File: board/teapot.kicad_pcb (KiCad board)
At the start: 2 copper layers, 49.9 x 50 mm, 41 parts, among them J1 MICROUSB, P1 BATT, P2 SMA, Q1 TEPT4400, U1 TPS79333DBVR, U2 TLV61225, U4 RFM69W, U5 STM32L052K8, U6 HTU21D, U7 MS5637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

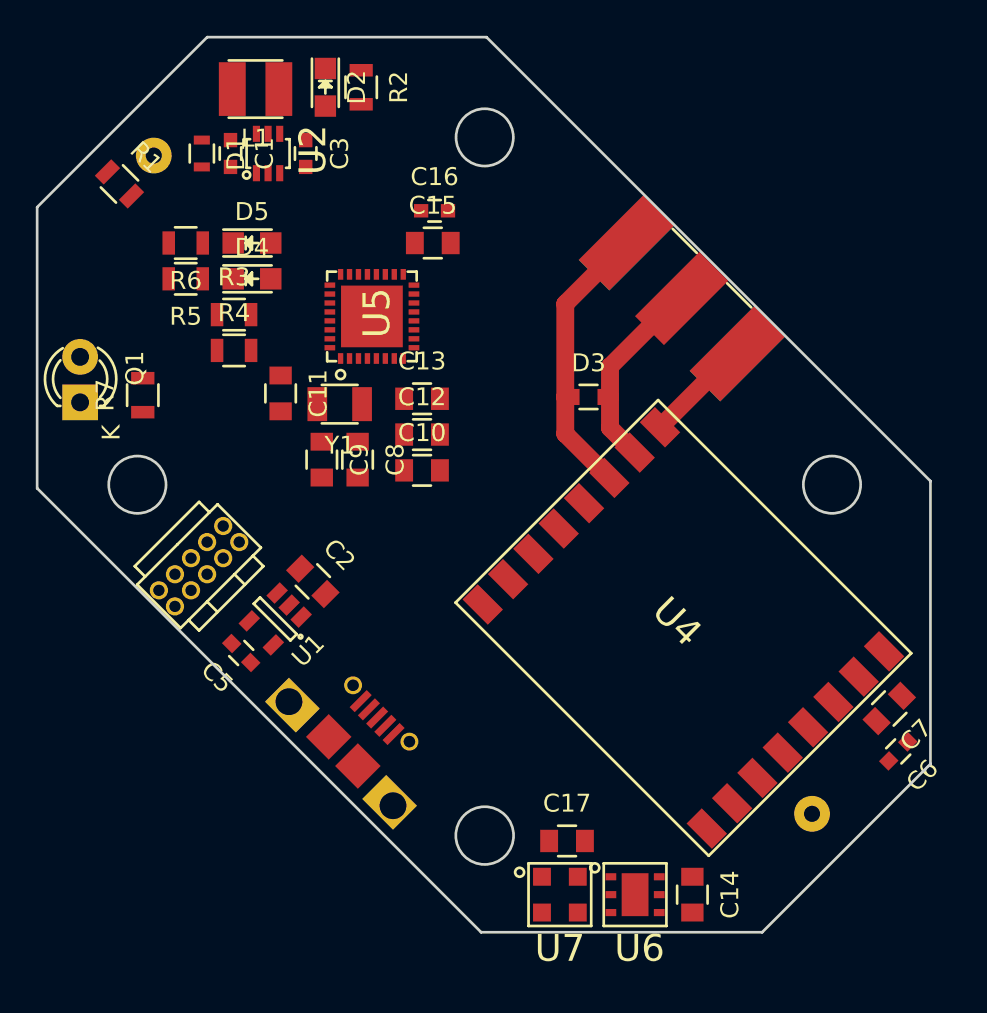
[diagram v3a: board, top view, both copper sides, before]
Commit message: Added test points and ANT PTH footprint
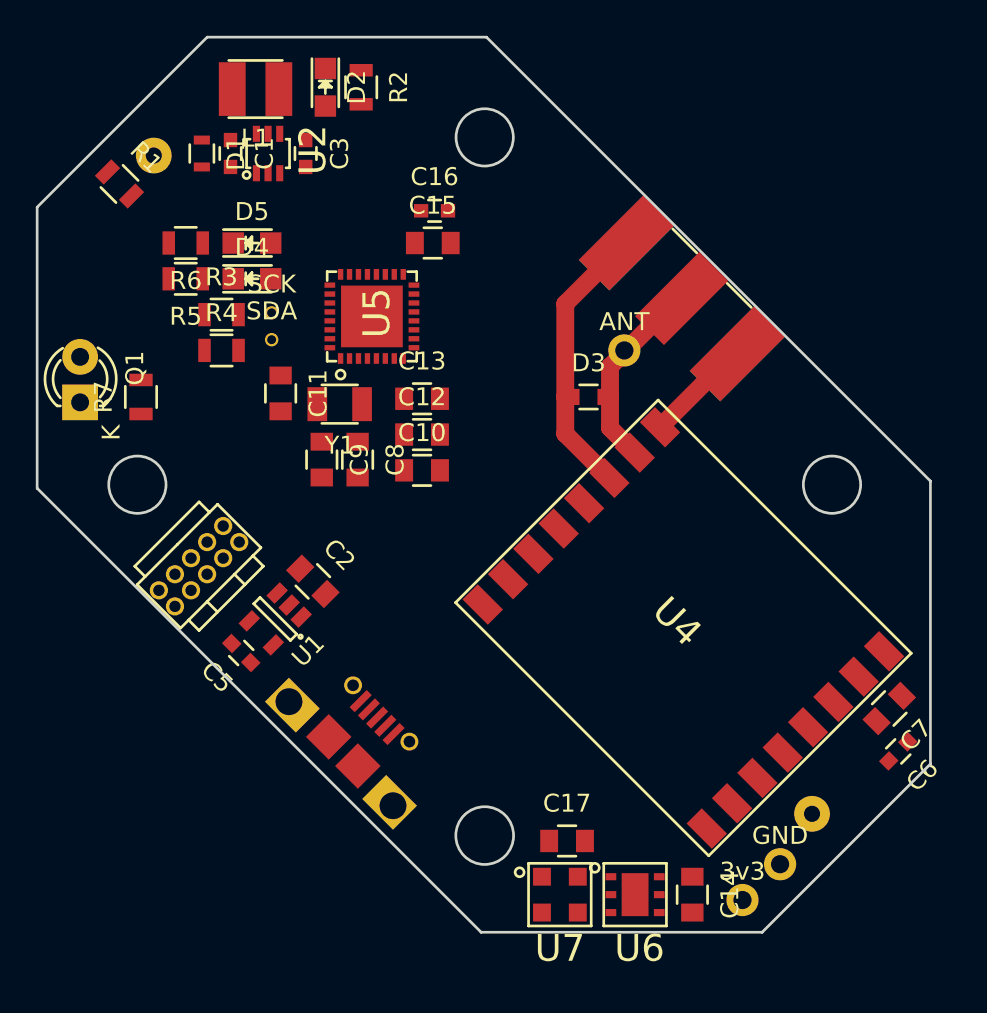
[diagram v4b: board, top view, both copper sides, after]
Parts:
- added TP1: ANT, footprints:Test_point, F.Cu at (134.8, 105.5)
- added TP2: 3v3, footprints:Test_point, F.Cu at (141.4, 136.2)
- added TP3: GND, footprints:Test_point, F.Cu at (143.5, 134.2)
- added TP4: SCK, footprints:Test_point_mini, F.Cu at (115.1, 103.4)
- added TP5: SDA, footprints:Test_point_mini, F.Cu at (115.1, 104.9)
- moved R3 0.70 mm to (112.3, 103.5)
- moved R4 0.70 mm to (112.3, 105.5)
- moved R7 0.14 mm to (107.8, 108.1)
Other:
- net class Default: clearance 0.2 -> 0.15
- rule trace_clearance: 0.2 -> 0.15
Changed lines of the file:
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@@
 (kicad_pcb (version 4) (host pcbnew 4.0.1-3.201512150931+6195~38~ubuntu14.04.1-stable)
   (general
-    (links 109)
-    (no_connects 104)
+    (links 114)
+    (no_connects 109)
     (area 101.924999 87.924999 151.975001 138.075001)
     (thickness 1.6)
@@
     (tracks 17)
     (zones 0)
-    (modules 41)
+    (modules 46)
     (nets 30)
   )
@@
     (user_trace_width 0.75)
     (user_trace_width 1)
-    (trace_clearance 0.2)
+    (trace_clearance 0.15)
     (zone_clearance 0.5)
     (zone_45_only no)
@@
   (net 29 "Net-(J1-PadS)")
   (net_class Default "This is the default net class."
-    (clearance 0.2)
+    (clearance 0.15)
     (trace_width 0.25)
     (via_dia 0.7)
@@
   )
   (module Resistors_SMD:R_0805 (layer F.Cu)
-    (at 113 103.5)
+    (at 112.3 103.5)
     (descr "Resistor SMD 0805, reflow soldering, Vishay (see dcrcw.pdf)")
     (tags "resistor 0805")
@@
   )
   (module Resistors_SMD:R_0805 (layer F.Cu)
-    (at 113 105.5)
+    (at 112.3 105.5)
     (descr "Resistor SMD 0805, reflow soldering, Vishay (see dcrcw.pdf)")
     (tags "resistor 0805")
@@
   )
   (module Resistors_SMD:R_0805 (layer F.Cu)
-    (at 107.9 108 90)
+    (at 107.8 108.1 90)
     (descr "Resistor SMD 0805, reflow soldering, Vishay (see dcrcw.pdf)")
     (tags "resistor 0805")
@@
       (net 29 "Net-(J1-PadS)"))
   )
+  (module footprints:Test_point (layer F.Cu)
+    (at 134.8 105.5)
+    (descr "Test Point")
+    (tags "test point")
+    (fp_text reference TP1 (at 0 2) (layer F.SilkS) hide
+      (effects (font (size 1 1) (thickness 0.15)))
+    )
+    (fp_text value ANT (at 0 -1.6) (layer F.SilkS)
+      (effects (font (size 1 1) (thickness 0.15)))
+    )
+    (pad 1 thru_hole circle (at 0 0) (size 1.8 1.8) (drill 1.016) (layers *.Cu *.Mask F.SilkS)
+      (net 16 "Net-(D3-Pad2)"))
+    (model Pin_Headers.3dshapes/Pin_Header_Straight_1x01.wrl
+      (at (xyz 0 0 0))
+      (scale (xyz 1 1 1))
+      (rotate (xyz 0 0 90))
+    )
+  )
+  (module footprints:Test_point (layer F.Cu)
+    (at 141.4 136.2)
+    (descr "Test Point")
+    (tags "test point")
+    (fp_text reference TP2 (at 0 2) (layer F.SilkS) hide
+      (effects (font (size 1 1) (thickness 0.15)))
+    )
+    (fp_text value 3v3 (at 0 -1.6) (layer F.SilkS)
+      (effects (font (size 1 1) (thickness 0.15)))
+    )
+    (pad 1 thru_hole circle (at 0 0) (size 1.8 1.8) (drill 1.016) (layers *.Cu *.Mask F.SilkS)
+      (net 1 +3V3))
+    (model Pin_Headers.3dshapes/Pin_Header_Straight_1x01.wrl
+      (at (xyz 0 0 0))
+      (scale (xyz 1 1 1))
+      (rotate (xyz 0 0 90))
+    )
+  )
+  (module footprints:Test_point (layer F.Cu)
+    (at 143.5 134.2)
+    (descr "Test Point")
+    (tags "test point")
+    (fp_text reference TP3 (at 0 2) (layer F.SilkS) hide
+      (effects (font (size 1 1) (thickness 0.15)))
+    )
+    (fp_text value GND (at 0 -1.6) (layer F.SilkS)
+      (effects (font (size 1 1) (thickness 0.15)))
+    )
+    (pad 1 thru_hole circle (at 0 0) (size 1.8 1.8) (drill 1.016) (layers *.Cu *.Mask F.SilkS)
+      (net 3 GND))
+    (model Pin_Headers.3dshapes/Pin_Header_Straight_1x01.wrl
+      (at (xyz 0 0 0))
+      (scale (xyz 1 1 1))
+      (rotate (xyz 0 0 90))
+    )
+  )
+  (module footprints:Test_point_mini (layer F.Cu)
+    (at 115.1 103.4)
+    (descr "Test Point")
+    (tags "test point")
+    (fp_text reference TP4 (at 0 2) (layer F.SilkS) hide
+      (effects (font (size 1 1) (thickness 0.15)))
+    )
+    (fp_text value SCK (at 0 -1.6) (layer F.SilkS)
+      (effects (font (size 1 1) (thickness 0.15)))
+    )
+    (pad 1 thru_hole circle (at 0 0) (size 0.75 0.75) (drill 0.5) (layers *.Cu *.Mask F.SilkS)
+      (net 7 /I2C_SCK))
+    (model Pin_Headers.3dshapes/Pin_Header_Straight_1x01.wrl
+      (at (xyz 0 0 0))
+      (scale (xyz 1 1 1))
+      (rotate (xyz 0 0 90))
+    )
+  )
+  (module footprints:Test_point_mini (layer F.Cu)
+    (at 115.1 104.9)
+    (descr "Test Point")
+    (tags "test point")
+    (fp_text reference TP5 (at 0 2) (layer F.SilkS) hide
+      (effects (font (size 1 1) (thickness 0.15)))
+    )
+    (fp_text value SDA (at 0 -1.6) (layer F.SilkS)
+      (effects (font (size 1 1) (thickness 0.15)))
+    )
+    (pad 1 thru_hole circle (at 0 0) (size 0.75 0.75) (drill 0.5) (layers *.Cu *.Mask F.SilkS)
+      (net 8 /I2C_SDA))
+    (model Pin_Headers.3dshapes/Pin_Header_Straight_1x01.wrl
+      (at (xyz 0 0 0))
+      (scale (xyz 1 1 1))
+      (rotate (xyz 0 0 90))
+    )
+  )
   (gr_line (start 126.8 138) (end 142.5 138) (angle 90) (layer Edge.Cuts) (width 0.15))

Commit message: Changed all 0805 (except LEDs) to 0603
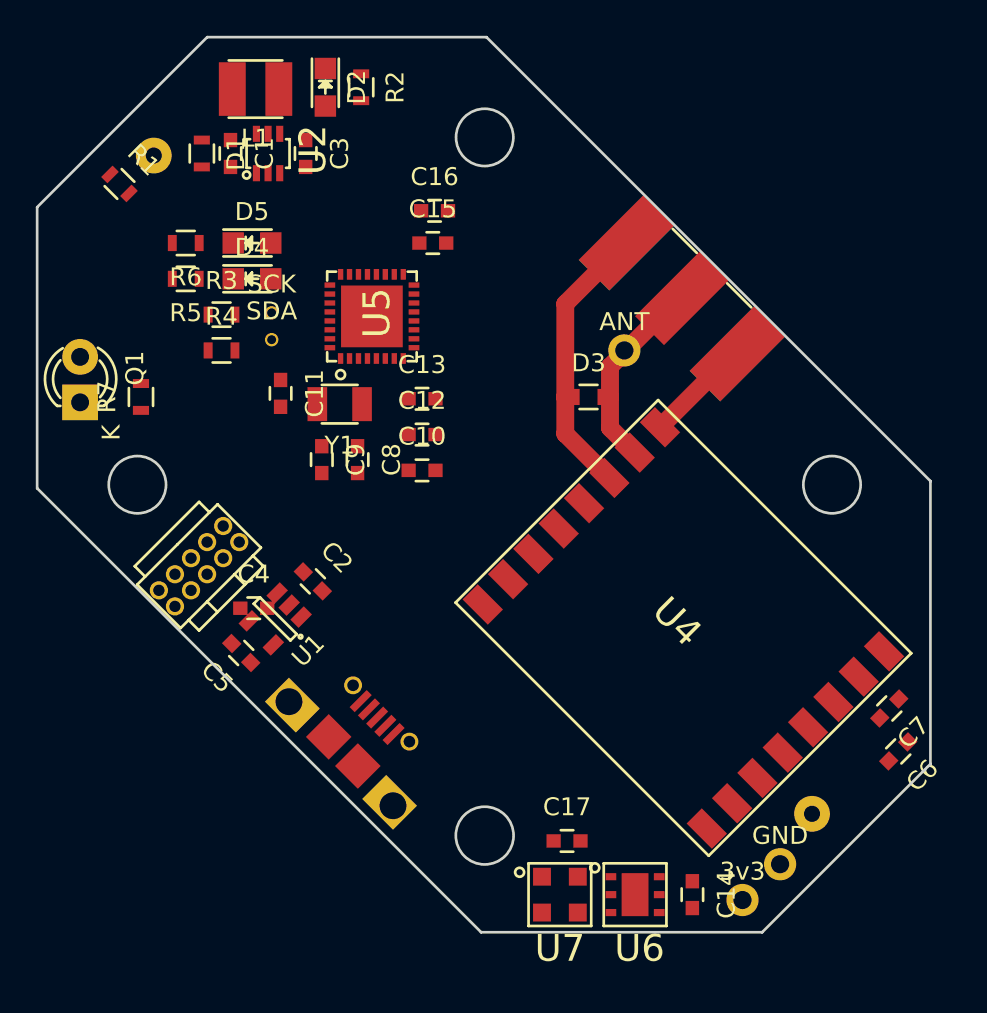
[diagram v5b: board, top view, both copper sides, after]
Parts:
- added C4: 10n, Capacitors_SMD:C_0603, F.Cu at (114.1, 119.9)
- C10, C11, C12, C13, C14, C15, C17, C2, C7, C8, C9: footprint Capacitors_SMD:C_0805 -> Capacitors_SMD:C_0603
- R1, R2, R3, R4, R5, R6, R7: footprint Resistors_SMD:R_0805 -> Resistors_SMD:R_0603
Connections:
- U1 pad 4: (no net) -> Net-(C4-Pad1)

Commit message: 0603 test placement
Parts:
- moved C6 10.8 mm to (148.4, 117.2), turned to 45 degrees
- moved C7 7.20 mm to (149.5, 118.3), turned to 45 degrees
- moved C4 5.03 mm to (118.2, 117.0), turned to 180 degrees
- moved C2 3.73 mm to (121.0, 119.5), turned to 270 degrees
- moved C5 3.57 mm to (115.5, 119.5), turned to 90 degrees
- moved U1 3.10 mm to (118.2, 119.5), turned to 180 degrees
- moved C11 1.30 mm to (115.6, 106.6), turned to 180 degrees
- moved C10 1.20 mm to (123.6, 111.0)
- moved R1 0.73 mm to (106.8, 96.9), turned to 90 degrees
- moved C12 0.71 mm to (123.6, 109.5)
- moved R4 0.71 mm to (112.8, 105.0)
- moved R3 0.51 mm to (112.8, 103.4)
- moved R5 0.36 mm to (110.6, 101.3)
- moved R6 0.36 mm to (110.6, 99.7)
- moved C9 0.36 mm to (118.2, 111.4)
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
